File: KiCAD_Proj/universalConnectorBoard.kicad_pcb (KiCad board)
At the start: 2 copper layers, 28 parts, among them IC1 RPI_Pico_EvaluationBoard, IC2 SN74LV4052ADR, J1 691401700003B, J2 Display1, J3 Display2, J4 RPI4, J5 Ledstrip2, J6 MUX3_UART, J7 MUX4_UART, J8 Ledstrip1, U2 LM1117DT-3.3, U3 TMC2209_MotorDriver, U4 TMC2209_MotorDriver

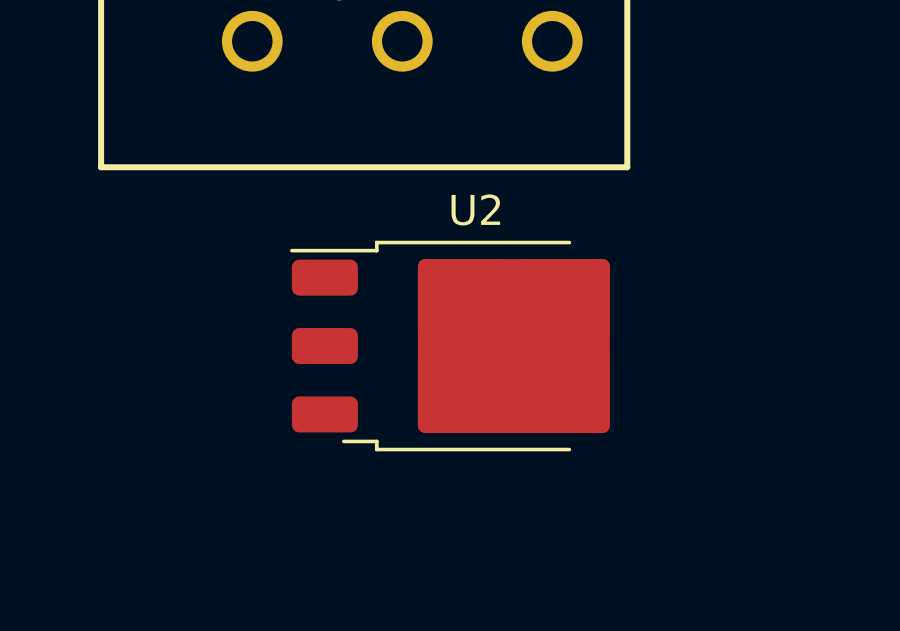
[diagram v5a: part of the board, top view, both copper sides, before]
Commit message: Added power management
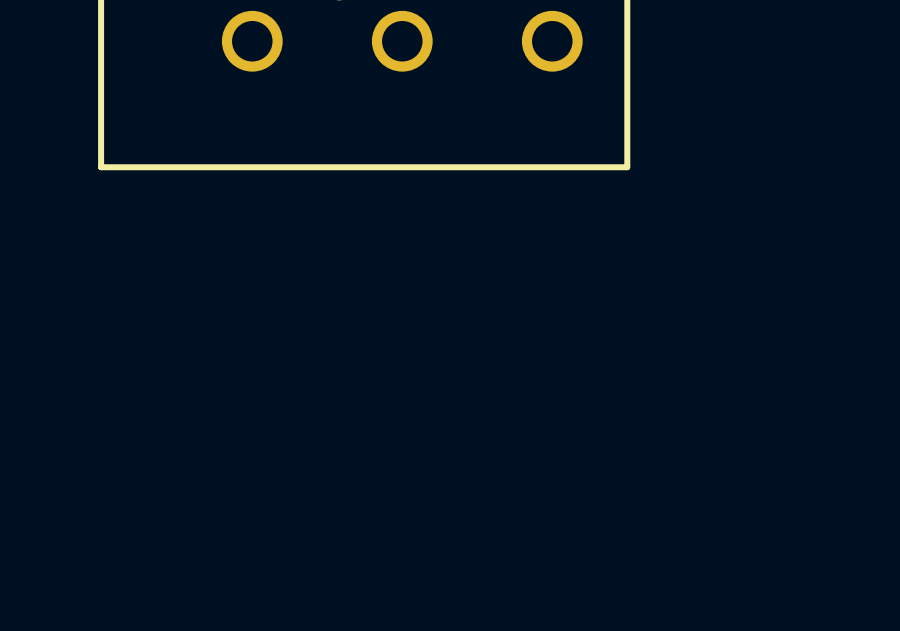
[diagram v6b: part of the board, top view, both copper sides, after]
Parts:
- removed U2: LM1117DT-3.3, Package_TO_SOT_SMD:TO-252-3_TabPin2
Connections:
- IC1 pad 22: unconnected-(IC1-GPIO17-Pad22) -> /MD2_DIR
- IC1 pad 24: unconnected-(IC1-GPIO18-Pad24) -> /MD2_STEP
- IC1 pad 25: unconnected-(IC1-GPIO19-Pad25) -> /MD2_EN
- IC1 pad 26: unconnected-(IC1-GPIO20-Pad26) -> /MD1_DIR
- IC1 pad 27: unconnected-(IC1-GPIO21-Pad27) -> /MD1_STEP
- IC1 pad 29: unconnected-(IC1-GPIO22-Pad29) -> /MD1_EN

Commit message: Schematic nearly done, ordened
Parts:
- added C10: 0.1uF, Capacitor_SMD:C_0603_1608Metric_Pad1.08x0.95mm_HandSolder, F.Cu at (252.0, 104.1)
- added C11: 47µF, Capacitor_SMD:C_0603_1608Metric_Pad1.08x0.95mm_HandSolder, F.Cu at (252.0, 106.6)
- added C12: 47µF, Capacitor_SMD:C_0603_1608Metric_Pad1.08x0.95mm_HandSolder, F.Cu at (256.4, 91.6)
- added C13: 47µF, Capacitor_SMD:C_0603_1608Metric_Pad1.08x0.95mm_HandSolder, F.Cu at (256.4, 94.1)
- added C14: 47µF, Capacitor_SMD:C_0603_1608Metric_Pad1.08x0.95mm_HandSolder, F.Cu at (256.4, 96.6)
- added C4: 1uF, Capacitor_SMD:C_0603_1608Metric_Pad1.08x0.95mm_HandSolder, F.Cu at (260.8, 71.1)
- added C5: 22uF, Capacitor_SMD:C_0603_1608Metric_Pad1.08x0.95mm_HandSolder, F.Cu at (252.0, 91.6)
- added C6: 22uF, Capacitor_SMD:C_0603_1608Metric_Pad1.08x0.95mm_HandSolder, F.Cu at (252.0, 94.1)
- added C7: 0.1uF, Capacitor_SMD:C_0603_1608Metric_Pad1.08x0.95mm_HandSolder, F.Cu at (252.0, 96.6)
- added C8: 0.1uF, Capacitor_SMD:C_0603_1608Metric_Pad1.08x0.95mm_HandSolder, F.Cu at (252.0, 99.1)
- added C9: 100pF, Capacitor_SMD:C_0603_1608Metric_Pad1.08x0.95mm_HandSolder, F.Cu at (252.0, 101.6)
- added IC3: TPS51397ARJER, Healthbot-Footprints:QFN45P300X300X100-21N-D, F.Cu at (261.2, 67.2)
- added IC4: TCA9534DWR, SamacSys_Parts:SOIC127P1030X265-16N, F.Cu at (231.1, 109.9)
- added J1: 691401700003B, SamacSys_Parts:691401700003B, F.Cu at (244.5, 69.2)
- added J10: Cheeks, Connector_JST:JST_XH_S2B-XH-A_1x02_P2.50mm_Horizontal, F.Cu at (237.5, 93.6)
- added J9: Mouth, Connector_JST:JST_XH_S2B-XH-A_1x02_P2.50mm_Horizontal, F.Cu at (228.1, 93.6)
- added L1: 1.8uH, Inductor_SMD:L_0603_1608Metric_Pad1.05x0.95mm_HandSolder, F.Cu at (256.4, 99.1)
- added PS1: TSR_1-2433, SamacSys_Parts:TSR-1-2433, F.Cu at (244.4, 81.2)
- added R11: 0, Resistor_SMD:R_0603_1608Metric_Pad0.98x0.95mm_HandSolder, F.Cu at (256.4, 101.6)
- added R12: 100k, Resistor_SMD:R_0603_1608Metric_Pad0.98x0.95mm_HandSolder, F.Cu at (256.4, 104.1)
- added R13: 330k, Resistor_SMD:R_0603_1608Metric_Pad0.98x0.95mm_HandSolder, F.Cu at (256.4, 106.6)
- added R14: 15k, Resistor_SMD:R_0603_1608Metric_Pad0.98x0.95mm_HandSolder, F.Cu at (260.7, 91.6)
- added R15: 51.1, Resistor_SMD:R_0603_1608Metric_Pad0.98x0.95mm_HandSolder, F.Cu at (260.7, 94.1)
- added R16: 110k, Resistor_SMD:R_0603_1608Metric_Pad0.98x0.95mm_HandSolder, F.Cu at (260.7, 96.6)
- added R17: 15k, Resistor_SMD:R_0603_1608Metric_Pad0.98x0.95mm_HandSolder, F.Cu at (260.7, 99.1)
- added R18: 0, Resistor_SMD:R_0603_1608Metric_Pad0.98x0.95mm_HandSolder, F.Cu at (260.7, 101.6)
- added R19: 10k, Resistor_SMD:R_0603_1608Metric_Pad0.98x0.95mm_HandSolder, F.Cu at (245.7, 91.6)
- added R20: 10k, Resistor_SMD:R_0603_1608Metric_Pad0.98x0.95mm_HandSolder, F.Cu at (245.7, 94.1)
- added R21: 10k, Resistor_SMD:R_0603_1608Metric_Pad0.98x0.95mm_HandSolder, F.Cu at (245.7, 96.6)
- added R22: R, Resistor_SMD:R_0603_1608Metric_Pad0.98x0.95mm_HandSolder, F.Cu at (245.7, 99.1)
- added R23: R, Resistor_SMD:R_0603_1608Metric_Pad0.98x0.95mm_HandSolder, F.Cu at (245.7, 101.6)
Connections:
- C1 pad 1: Net-(IC2-VCC) -> /VCC_MUX
- C1 pad 2: GND -> +12V
- C2 pad 1: GND -> +12V
- C3 pad 1: GND -> +12V
- IC1 pad 13: GND -> +12V
- IC1 pad 18: GND -> +12V
- IC1 pad 22: /MD2_DIR -> /Radar_CS
- IC1 pad 23: GND -> +12V
- IC1 pad 24: /MD2_STEP -> /Radar_RES
- IC1 pad 25: /MD2_EN -> /MD1_STEP
- IC1 pad 27: /MD1_STEP -> /MD2_STEP
- IC1 pad 28: GND -> +12V
- IC1 pad 29: /MD1_EN -> /MD2_DIR
- IC1 pad 3: GND -> +12V
- IC1 pad 31: unconnected-(IC1-GPIO26_ADC0-Pad31) -> /IOexp_SDA
- IC1 pad 32: unconnected-(IC1-GPIO27_ADC1-Pad32) -> /IOexp_SCL
- IC1 pad 34: unconnected-(IC1-GPIO28_ADC2-Pad34) -> /IOexp_INT
- IC1 pad 38: GND -> +12V
- IC1 pad 4: /LED_Cheeks -> /STOP_PIN1
- IC1 pad 42: GND -> +12V
- IC1 pad 5: /LED_Mouth -> /STOP_PIN2
- IC1 pad 8: GND -> +12V
- IC2 pad 16: Net-(IC2-VCC) -> /VCC_MUX
- IC2 pad 7: GND -> +12V
- IC2 pad 8: GND -> +12V
- J2 pad 6: GND -> +12V
- J3 pad 6: GND -> +12V
- J4 pad 14: GND -> +12V
- J4 pad 20: GND -> +12V
- J4 pad 25: GND -> +12V
- J4 pad 30: GND -> +12V
- J4 pad 34: GND -> +12V
- J4 pad 39: GND -> +12V
- J4 pad 6: GND -> +12V
- J4 pad 9: GND -> +12V
- J5 pad 1: GND -> +12V
- J6 pad 1: VCC -> /VCC_MUX
- J6 pad 4: GND -> +12V
- J7 pad 1: VCC -> /VCC_MUX
- J7 pad 4: GND -> +12V
- J8 pad 1: GND -> +12V
- J8 pad 2: GND -> +12V
- JP2 pad 2: Net-(IC2-VCC) -> /VCC_MUX
- R1 pad 1: VCC -> /VCC_MUX
- R2 pad 1: VCC -> /VCC_MUX
- R3 pad 1: VCC -> /VCC_MUX
- R4 pad 1: VCC -> /VCC_MUX
- R5 pad 1: VCC -> /VCC_MUX
- R6 pad 1: VCC -> /VCC_MUX
- R7 pad 1: VCC -> /VCC_MUX
- R8 pad 1: VCC -> /VCC_MUX
- U3 pad 1: GND -> +12V
- U3 pad 18: unconnected-(U3-DIAG-Pad18) -> /STOP_PIN1
- U3 pad 7: GND -> +12V
- U4 pad 1: GND -> +12V
- U4 pad 18: unconnected-(U4-DIAG-Pad18) -> /STOP_PIN2
- U4 pad 7: GND -> +12V

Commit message: Finished schematic, in review
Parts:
- removed the J1 at (193.2, 38.1)
- removed the J1 at (244.5, 69.2)
- removed the PS1 at (244.4, 81.2)
- removed the PS1 at (205.7, 63.5)
- removed the R22 at (245.7, 99.1)
- removed the R23 at (245.7, 101.6)
- removed U3, U4: TMC2209_MotorDriver, TMC2209_SILENTSTEPSTICK:MODULE_TMC2209_SILENTSTEPSTICK
- added C15: 100uF 50V, Capacitor_SMD:CP_Elec_8x10, F.Cu at (139.7, 73.7)
- added C16: 100nF 50V, Capacitor_SMD:C_0805_2012Metric_Pad1.18x1.45mm_HandSolder, F.Cu at (163.4, 81.3)
- added C17: 100uF 50V, Capacitor_SMD:CP_Elec_8x10, F.Cu at (152.4, 73.7)
- added C18: 100nF 50V, Capacitor_SMD:C_0805_2012Metric_Pad1.18x1.45mm_HandSolder, F.Cu at (147.3, 81.3)
- added C19: 0.10μF, Capacitor_SMD:C_0603_1608Metric_Pad1.08x0.95mm_HandSolder, F.Cu at (155.2, 133.6)
- added C20: 0.10μF, Capacitor_SMD:C_0603_1608Metric_Pad1.08x0.95mm_HandSolder, F.Cu at (152.7, 133.6)
- added C21: 0.10μF, Capacitor_SMD:C_0603_1608Metric_Pad1.08x0.95mm_HandSolder, F.Cu at (150.1, 133.6)
- added D1: LED, LED_SMD:LED_0603_1608Metric_Pad1.05x0.95mm_HandSolder, F.Cu at (134.6, 138.0)
- added J1: 691401700003B, SamacSys_Parts:691401700003B, F.Cu at (176.6, 63.3)
- added J11: MD_SW1, Connector_JST:JST_XH_S2B-XH-A_1x02_P2.50mm_Horizontal, F.Cu at (184.5, 104.1)
- added J12: MD_SW2, Connector_JST:JST_XH_S2B-XH-A_1x02_P2.50mm_Horizontal, F.Cu at (184.5, 94.7)
- added J13: Motor1, Connector_JST:JST_XH_S4B-XH-A_1x04_P2.50mm_Horizontal, F.Cu at (141.0, 57.5)
- added J14: Motor2, Connector_JST:JST_XH_S4B-XH-A_1x04_P2.50mm_Horizontal, F.Cu at (156.3, 57.5)
- added JP1: Mux_Vcc, Connector_PinHeader_2.54mm:PinHeader_1x03_P2.54mm_Vertical, F.Cu at (172.7, 91.4)
- added JP3: Jumper_2_Open, Jumper:SolderJumper-2_P1.3mm_Open_RoundedPad1.0x1.5mm, F.Cu at (140.9, 81.2)
- added JP4: Jumper_2_Open, Jumper:SolderJumper-2_P1.3mm_Open_RoundedPad1.0x1.5mm, F.Cu at (154.2, 81.3)
- added JP5: Jumper_2_Open, Jumper:SolderJumper-2_P1.3mm_Open_RoundedPad1.0x1.5mm, F.Cu at (157.8, 81.3)
- added JP6: Ledstrip_VCC, Connector_PinHeader_2.54mm:PinHeader_1x03_P2.54mm_Vertical, F.Cu at (115.4, 133.8)
- added JP7: Ledstrip_VCC, Connector_PinHeader_2.54mm:PinHeader_1x03_P2.54mm_Vertical, F.Cu at (115.4, 138.4)
- added PS1: TSR_1-2433, SamacSys_Parts:TSR-1-2433, F.Cu at (185.4, 76.2)
- added Q1: 2N7002, Package_TO_SOT_SMD:SOT-23, F.Cu at (154.2, 138.2)
- added Q2: 2N7002, Package_TO_SOT_SMD:SOT-23, F.Cu at (149.7, 138.2)
- added Q3: BSS84, Package_TO_SOT_SMD:SOT-23, F.Cu at (145.3, 138.2)
- added R22: R, Resistor_SMD:R_0603_1608Metric_Pad0.98x0.95mm_HandSolder, F.Cu at (206.6, 137.2)
- added R22: 47, Resistor_SMD:R_0603_1608Metric_Pad0.98x0.95mm_HandSolder, F.Cu at (147.6, 133.6)
- added R23: 50k, Resistor_SMD:R_0603_1608Metric_Pad0.98x0.95mm_HandSolder, F.Cu at (145.1, 133.6)
- added R23: R, Resistor_SMD:R_0603_1608Metric_Pad0.98x0.95mm_HandSolder, F.Cu at (206.6, 139.7)
- added R24: 50k, Resistor_SMD:R_0603_1608Metric_Pad0.98x0.95mm_HandSolder, F.Cu at (206.6, 142.2)
- added R25: 50k, Resistor_SMD:R_0603_1608Metric_Pad0.98x0.95mm_HandSolder, F.Cu at (188.9, 129.5)
- added R26: 47, Resistor_SMD:R_0603_1608Metric_Pad0.98x0.95mm_HandSolder, F.Cu at (142.6, 133.6)
- added R27: 100, Resistor_SMD:R_0603_1608Metric_Pad0.98x0.95mm_HandSolder, F.Cu at (140.1, 133.6)
- added R28: 50k, Resistor_SMD:R_0603_1608Metric_Pad0.98x0.95mm_HandSolder, F.Cu at (137.6, 133.6)
- added R29: 75, Resistor_SMD:R_0603_1608Metric_Pad0.98x0.95mm_HandSolder, F.Cu at (135.1, 133.6)
- added R30: 100, Resistor_SMD:R_0603_1608Metric_Pad0.98x0.95mm_HandSolder, F.Cu at (132.6, 133.6)
- added REF**: MountingHole_2.7mm_M2.5, MountingHole:MountingHole_2.7mm_M2.5, F.Cu at (274.0, 100.4)
- added REF**: MountingHole_2.7mm_M2.5, MountingHole:MountingHole_2.7mm_M2.5, F.Cu at (216.0, 100.4)
- added REF**: MountingHole_2.7mm_M2.5, MountingHole:MountingHole_2.7mm_M2.5, F.Cu at (216.0, 50.9)
- added REF**: MountingHole_2.7mm_M2.5, MountingHole:MountingHole_2.7mm_M2.5, F.Cu at (274.0, 50.9)
- added SW1: SW_Push, Connector_PinHeader_2.54mm:PinHeader_1x02_P2.54mm_Vertical, F.Cu at (140.7, 138.1)
- added TP1: ~, TestPoint:TestPoint_Pad_D1.5mm, F.Cu at (179.4, 146.2)
- added U1: TMC2209_MotorDriver, TMC2209_SILENTSTEPSTICK:MODULE_TMC2209_SILENTSTEPSTICK, F.Cu at (160.0, 95.2)
- added U2: TMC2209_MotorDriver, TMC2209_SILENTSTEPSTICK:MODULE_TMC2209_SILENTSTEPSTICK, F.Cu at (142.2, 95.2)
- J4: footprint Connector_PinHeader_2.54mm:PinHeader_2x20_P2.54mm_Vertical_SMD -> Connector_PinHeader_2.54mm:PinHeader_2x20_P2.54mm_Vertical
- J6: value MUX3_UART -> Extra MUX_UART; footprint Connector_PinSocket_2.54mm:PinSocket_1x04_P2.54mm_Vertical -> Connector_PinHeader_2.54mm:PinHeader_2x04_P2.54mm_Vertical
- J7: value MUX4_UART -> Extra GPIO output; footprint Connector_PinSocket_2.54mm:PinSocket_1x04_P2.54mm_Vertical -> Connector_PinHeader_2.54mm:PinHeader_1x02_P2.54mm_Vertical
- JP2: value Jumper_3_Bridged12 -> Jumper_2_Open; footprint Connector_PinHeader_2.54mm:PinHeader_1x03_P2.54mm_Vertical -> Jumper:SolderJumper-2_P1.3mm_Open_RoundedPad1.0x1.5mm
- moved C4 117.1 mm to (162.4, 134.7)
- moved J4 114.2 mm to (220.9, 52.2), turned to 90 degrees
- moved C1 105.3 mm to (193.6, 134.7)
- moved C12 102.9 mm to (166.8, 142.2)
- moved C13 102.9 mm to (166.8, 144.7)
- moved C5 100.5 mm to (162.4, 137.2)
- moved C6 100.5 mm to (162.4, 139.7)
- moved C7 100.5 mm to (162.4, 142.2)
- moved C8 100.5 mm to (162.4, 144.7)
- moved R14 95.5 mm to (175.5, 134.7)
- moved R15 95.5 mm to (175.5, 137.2)
- moved R17 95.5 mm to (175.5, 142.2)
- moved R18 95.5 mm to (175.5, 144.7)
- moved R16 95.5 mm to (175.5, 139.7)
- moved C14 93.4 mm to (171.1, 134.7)
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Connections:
- net /PowerManagement/BST renamed /Regulator5V/BST
- net /PowerManagement/FB renamed /Regulator5V/FB
- net /PowerManagement/MODE renamed /Regulator5V/MODE
- net /PowerManagement/PGOOD renamed /Regulator5V/PGOOD
- net /PowerManagement/SW renamed /Regulator5V/SW
- net /PowerManagement/VCC renamed /Regulator5V/VCC
- C1 pad 2: +12V -> GND
- C2 pad 1: +12V -> GND
- C2 pad 2: +12V -> /VCC_STRIP
- C3 pad 1: +12V -> GND
- C3 pad 2: +5V -> /VCC_STRIP2
- IC1 pad 11: /Display_RES -> /Display_DC
- IC1 pad 13: +12V -> GND
- IC1 pad 14: /Display_DC -> /Display_SDA
- IC1 pad 15: /Display_SDA -> /Display_SCL
- IC1 pad 16: /Display_SCL -> /Display_RES
- IC1 pad 18: +12V -> GND
- IC1 pad 23: +12V -> GND
- IC1 pad 28: +12V -> GND
- IC1 pad 3: +12V -> GND
- IC1 pad 38: +12V -> GND
- IC1 pad 39: unconnected-(IC1-VSYS-Pad39) -> Net-(IC1-VSYS)
- IC1 pad 40: unconnected-(IC1-VBUS-Pad40) -> Net-(IC1-VBUS)
- IC1 pad 41: unconnected-(IC1-SWCLK-Pad41) -> /SWCLK
- IC1 pad 42: +12V -> GND
- IC1 pad 43: unconnected-(IC1-SWDIO-Pad43) -> /SWDIO
- IC1 pad 8: +12V -> GND
- IC2 pad 11: /MUX_TX4 -> /MUX_RX4
- IC2 pad 7: +12V -> GND
- IC2 pad 8: +12V -> GND
- IC4 pad 1: +12V -> GND
- IC4 pad 11: unconnected-(IC4-P6-Pad11) -> /MUX_GPIO6
- IC4 pad 12: unconnected-(IC4-P7-Pad12) -> /MUX_GPIO7
- IC4 pad 2: +12V -> GND
- IC4 pad 3: +12V -> GND
- IC4 pad 8: +12V -> GND
- J10 pad 1: /LED_Mouth -> Net-(J10-Pin_1)
- J2 pad 6: +12V -> GND
- J3 pad 6: +12V -> GND
- J4 pad 14: +12V -> GND
- J4 pad 18: unconnected-(J4-Pin_18-Pad18) -> /SWCLK
- J4 pad 20: +12V -> GND
- J4 pad 22: unconnected-(J4-Pin_22-Pad22) -> /SWDIO
- J4 pad 25: +12V -> GND
- J4 pad 30: +12V -> GND
- J4 pad 34: +12V -> GND
- J4 pad 36: unconnected-(J4-Pin_36-Pad36) -> Net-(J4-Pin_36)
- J4 pad 39: +12V -> GND
- J4 pad 6: +12V -> GND
- J4 pad 9: +12V -> GND
- J5 pad 1: +12V -> GND
- J5 pad 3: +5V -> /VCC_STRIP2
- J6 pad 2: /MUX_TX3 -> /MUX_RX4
- J6 pad 3: /MUX_RX3 -> /MUX_RX4
- J6 pad 4: +12V -> GND
- J7 pad 1: /VCC_MUX -> /MUX_GPIO6
- J7 pad 2: /MUX_TX4 -> /MUX_GPIO7
- J8 pad 1: +12V -> GND
- J8 pad 2: +12V -> GND
- J8 pad 4: +12V -> /VCC_STRIP
- J9 pad 1: /LED_Cheeks -> Net-(J9-Pin_1)
- JP2 pad 1: +3.3V -> /StepperMotors/3.3V+
- JP2 pad 2: /VCC_MUX -> Net-(JP2-B)
- R4 pad 2: /MUX_TX4 -> /MUX_RX4
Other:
- board outline added: 65 x 56.5 mm
